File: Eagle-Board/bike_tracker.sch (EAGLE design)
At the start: 16 parts, among them J1 TRANSFLASH-LOCK

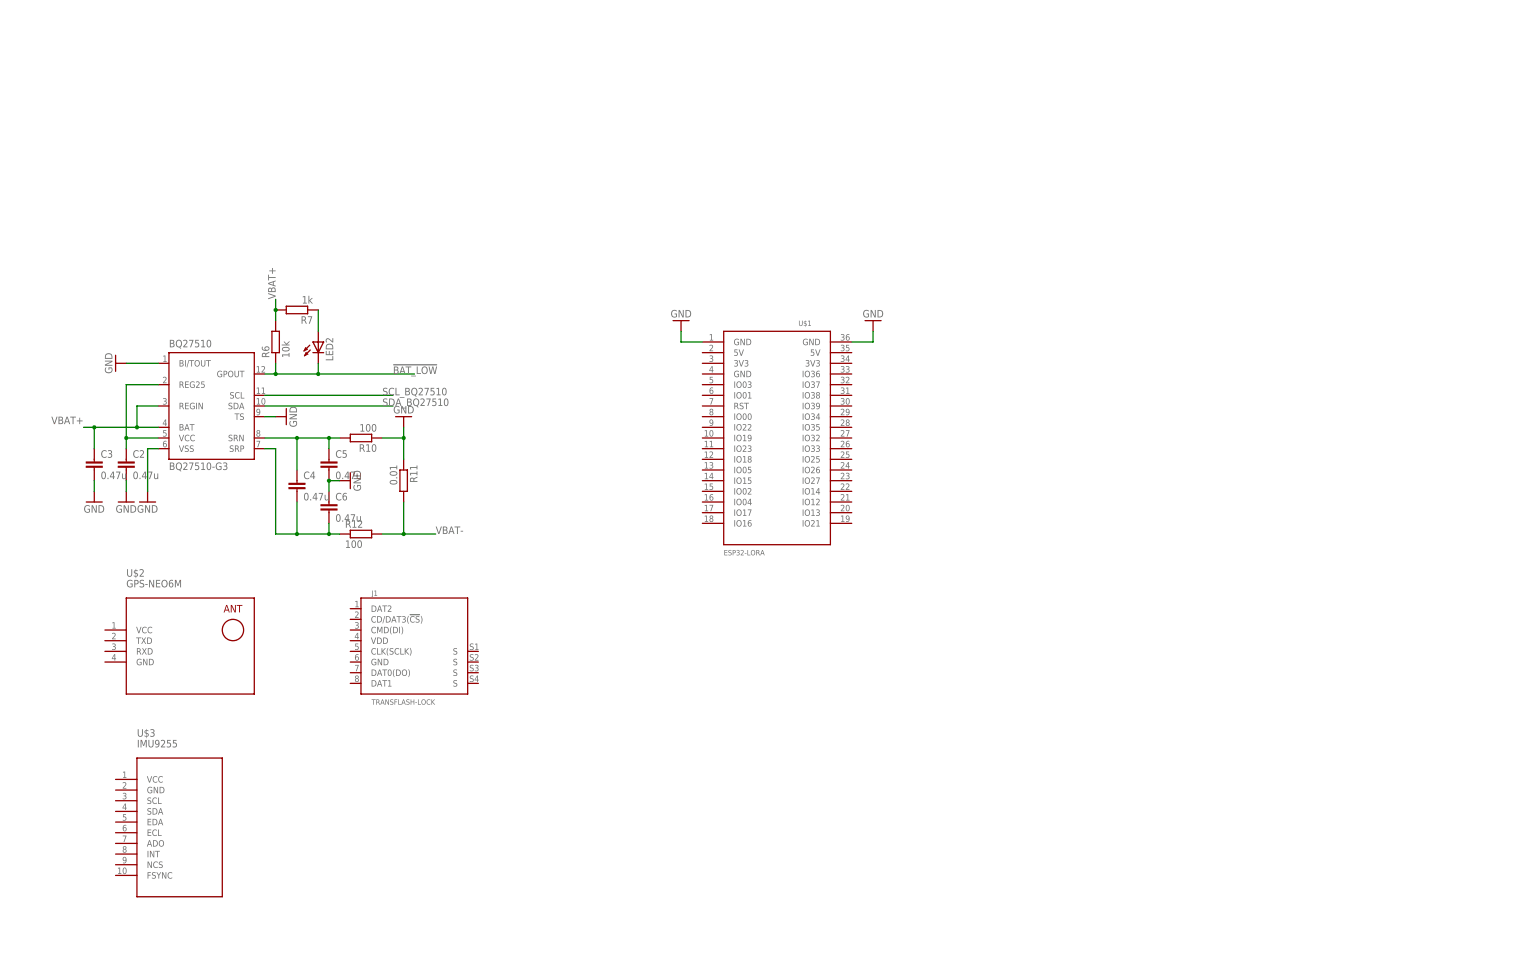
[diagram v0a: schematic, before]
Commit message: board design ready - revising and exporting for gerber - SeeedStudio Fusion files added
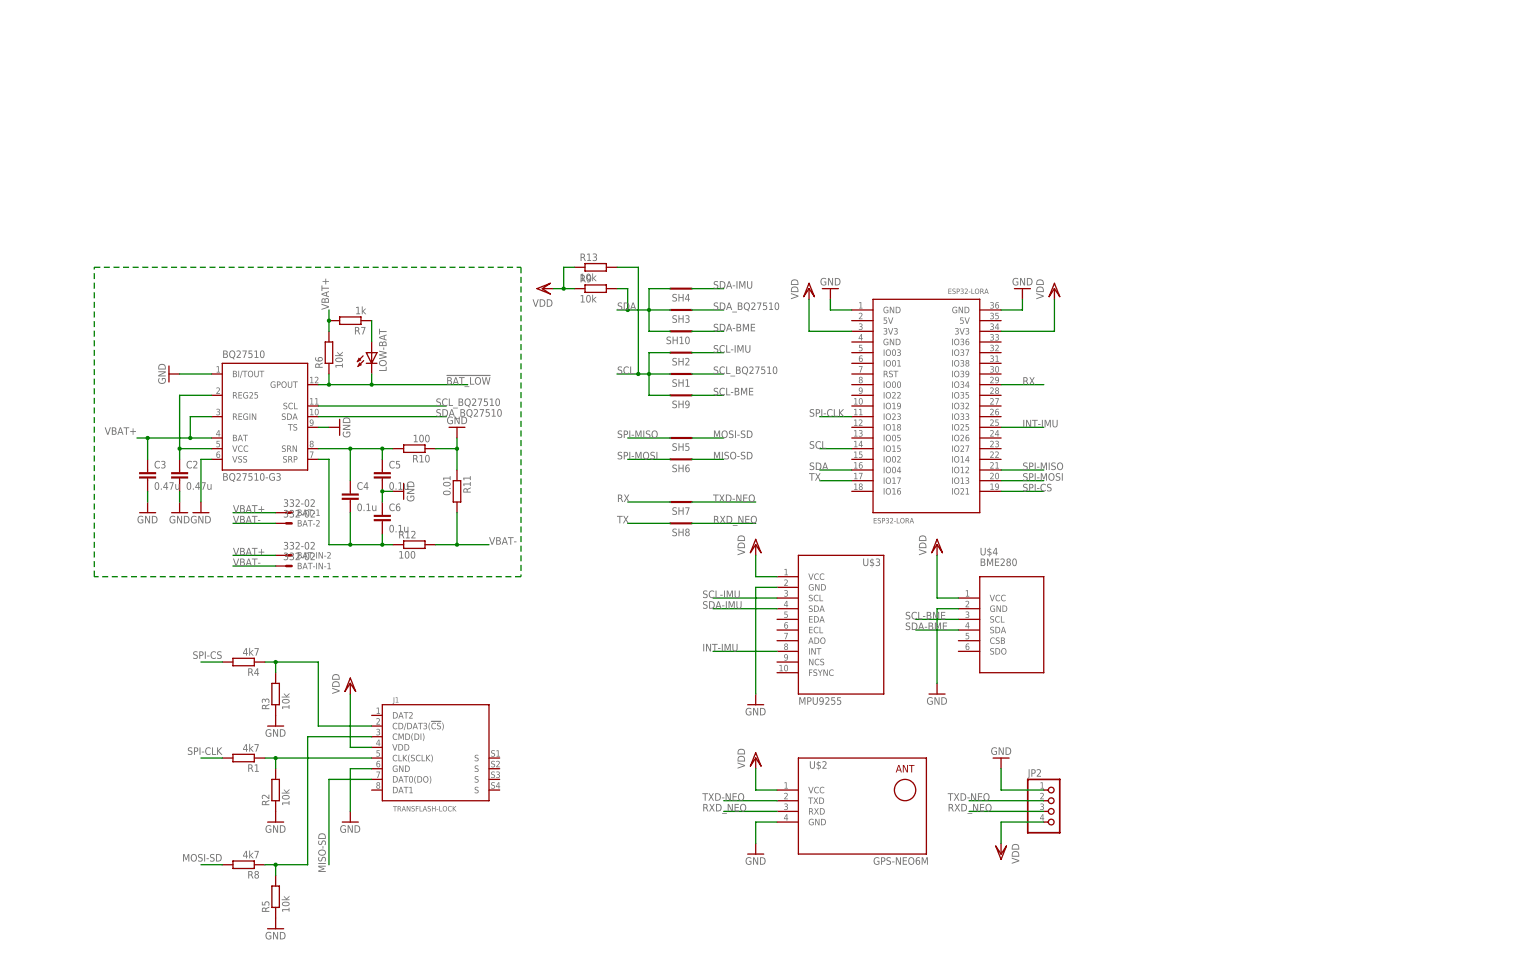
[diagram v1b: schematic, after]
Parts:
- removed LED2: (no value), led:LEDSML0805
- removed U$1: ESP32LORA, ESP32-DEVKITC:ESP32LORA
- added BAT, BAT-IN: 332-02, con-garry:332-02
- added ESP32-LORA: ESP32LORA, ESP32-DEVKITC:ESP32LORA
- added JP2: (no value), pinhead:PINHD-1X4
- added LOW-BAT: (no value), led:LEDSML0805
- added R1, R4, R8: 4k7, resistor:R-EU_R0603
- added R13, R2, R3, R5, R9: 10k, resistor:R-EU_R0603
- added SH1, SH10, SH2, SH3, SH4, SH5, SH6, SH7, SH8, SH9: SHORTT5, shorts:SHORTT5
- added U$4: BME280, diy-modules:BME280
- C4, C5, C6: value 0.47u -> 0.1u
- U$3: value IMU9255 -> MPU9255; device diy-modules:IMU9255 -> diy-modules:MPU9255
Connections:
- new net INT-IMU: ESP32-LORA.IO25, U$3.INT
- new net MISO-SD: J1.DAT0(DO), SH6.P$1
- new net MOSI-SD: R8.2, SH5.P$1
- new net N$1: J1.CLK(SCLK), R1.1, R2.2
- new net N$2: J1.CD/DAT3(!CS!), R3.2, R4.1
- new net N$3: J1.CMD(DI), R5.2, R8.1
- new net RX: ESP32-LORA.IO34, SH7.P$2
- new net RXD_NEO: JP2.3, SH8.P$1, U$2.RXD
- new net SCL: ESP32-LORA.IO15, R13.2, SH1.P$2, SH2.P$2, SH9.P$2
- new net SCL-BME: SH9.P$1, U$4.SCL
- new net SCL-IMU: SH2.P$1, U$3.SCL
- new net SDA: ESP32-LORA.IO04, R9.2, SH10.P$2, SH3.P$2, SH4.P$2
- new net SDA-BME: SH10.P$1, U$4.SDA
- new net SDA-IMU: SH4.P$1, U$3.SDA
- new net SPI-CLK: ESP32-LORA.IO23, R1.2
- new net SPI-CS: ESP32-LORA.IO21, R4.2
- new net SPI-MISO: ESP32-LORA.IO12, SH5.P$2
- new net SPI-MOSI: ESP32-LORA.IO13, SH6.P$2
- new net TX: ESP32-LORA.IO17, SH8.P$2
- new net TXD-NEO: JP2.2, SH7.P$1, U$2.TXD
- new net VDD: ESP32-LORA.3V3@3, ESP32-LORA.3V3@34, J1.VDD, JP2.4, R13.1, R9.1, U$2.VCC, U$3.VCC, U$4.VCC
- net !BAT_LOW: now also LOW-BAT.C; no longer LED2.C
- net GND: now also ESP32-LORA.GND@1, ESP32-LORA.GND@36, J1.GND, JP2.1, R2.1, R3.1, R5.1, U$2.GND, U$3.GND, U$4.GND; no longer U$1.GND@1, U$1.GND@36
- net N$9: now also LOW-BAT.A; no longer LED2.A
- net SCL_BQ27510: now also SH1.P$1
- net SDA_BQ27510: now also SH3.P$1
- net VBAT+: now also BAT-1.S, BAT-IN-2.S
- net VBAT-: now also BAT-2.S, BAT-IN-1.S
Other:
- moved on the sheet: BQ27510, C2, C3, C4, C5, C6, J1, R10, R11, R12, R6, R7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

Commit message: texas and switch libraries added final version with buttons and possibility to switch off/on external devices
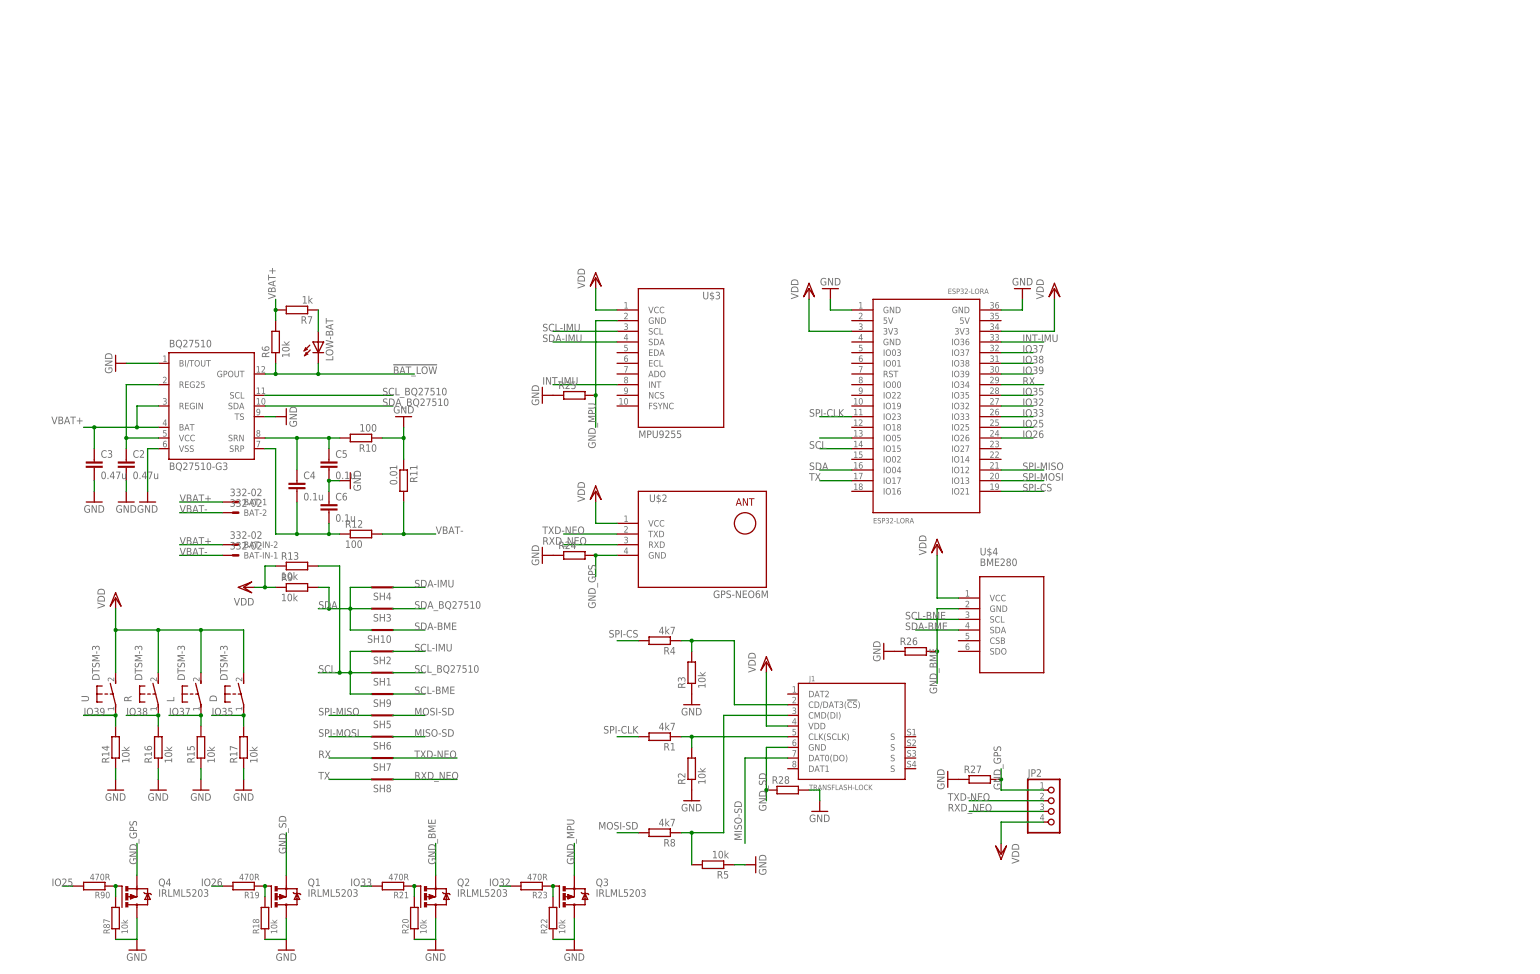
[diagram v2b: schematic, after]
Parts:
- added D, L, R, U: DTSM-3, switch-tact:DTSM-3
- added Q1, Q2, Q3, Q4: IRLML5203, transistor-power:IRLML5203
- added R14, R15, R16, R17: 10k, resistor:R-EU_R0603
- added R18, R20, R22, R87: 10k, ssmd:R_SMDR0603
- added R19, R21, R23, R90: 470R, ssmd:R_SMDR0603
- added R24, R25, R26, R27, R28: (no value), resistor:R-EU_R0201
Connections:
- new net GND_BME: Q2.S, R26.2, U$4.GND
- new net GND_GPS: JP2.1, Q4.S, R24.2, R27.2, U$2.GND
- new net GND_MPU: Q3.S, R25.2, U$3.GND
- new net GND_SD: J1.GND, Q1.S, R28.1
- new net IO25: ESP32-LORA.IO25, R90.2
- new net IO26: ESP32-LORA.IO26, R19.2
- new net IO32: ESP32-LORA.IO32, R23.2
- new net IO33: ESP32-LORA.IO33, R21.2
- new net IO35: D.1, ESP32-LORA.IO35, R17.2
- new net IO37: ESP32-LORA.IO37, L.1, R15.2
- new net IO38: ESP32-LORA.IO38, R.1, R16.2
- new net IO39: ESP32-LORA.IO39, R14.2, U.1
- new net N$12: ESP32-LORA.IO05
- new net N$4: Q4.G, R87.2, R90.1
- new net N$5: Q1.G, R18.2, R19.1
- new net N$6: Q2.G, R20.2, R21.1
- new net N$8: Q3.G, R22.2, R23.1
- net GND: now also Q1.D, Q2.D, Q3.D, Q4.D, R14.1, R15.1, R16.1, R17.1, R18.1, R20.1, R22.1, R24.1, R25.1, R26.1, R27.1, R28.2, R87.1; no longer J1.GND, JP2.1, U$2.GND, U$3.GND, U$4.GND
- net INT-IMU: now also ESP32-LORA.IO36; no longer ESP32-LORA.IO25
- net VDD: now also D.2, L.2, R.2, U.2
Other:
- moved on the sheet: BAT-1, BAT-2, BAT-IN-1, BAT-IN-2, BQ27510, C2, C3, C4, C5, C6, J1, LOW-BAT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

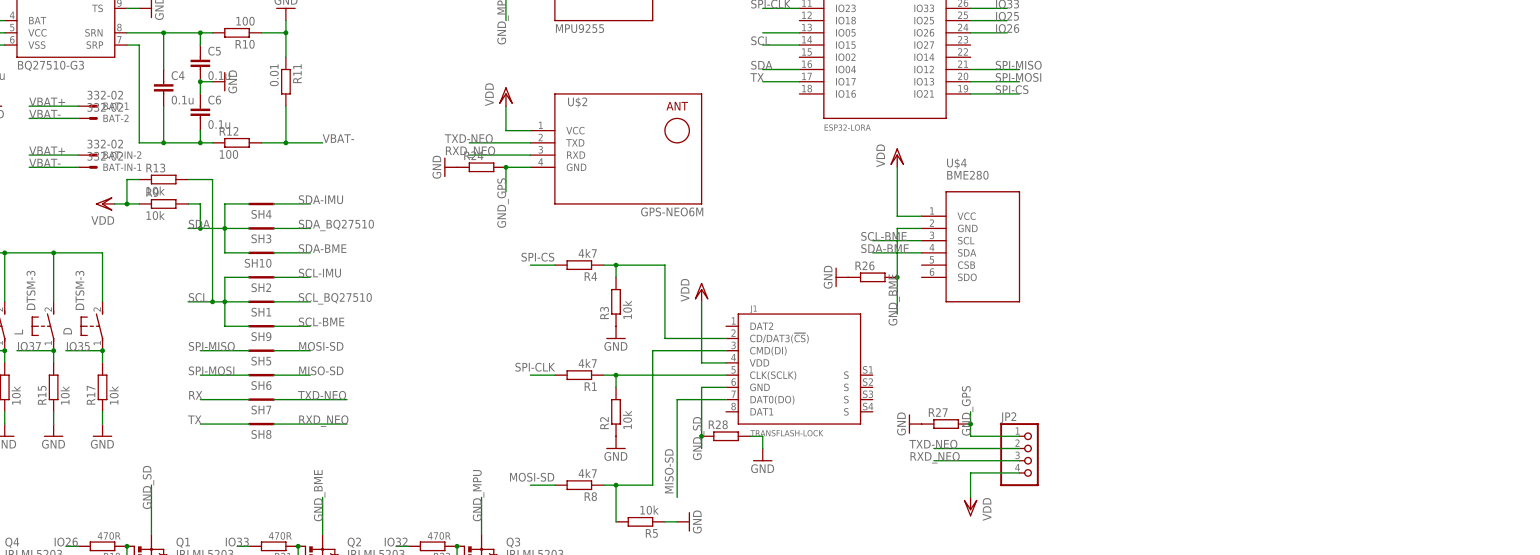
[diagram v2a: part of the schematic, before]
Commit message: updated rev1.1 -> added RTC chip (DS1339)
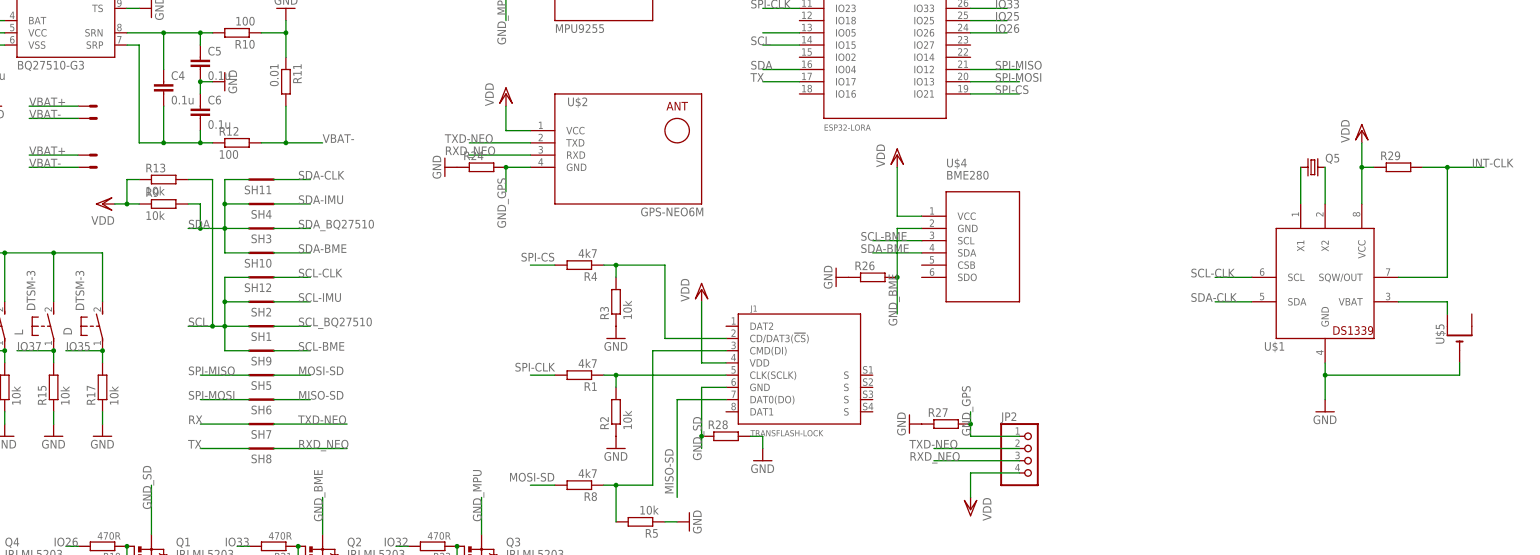
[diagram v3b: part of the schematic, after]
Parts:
- added Q5: (no value), adafruit:CRYSTALTC26H
- added R29: (no value), resistor:R-EU_R0603
- added SH11, SH12: SHORT, shorts:SHORT
- added U$1: DS1339, adafruit:DS1339
- added U$5: (no value), adafruit:CR1220SMT
- SH1, SH10, SH2, SH3, SH4, SH5, SH6, SH7, SH8, SH9: value SHORTT5 -> SHORT; device shorts:SHORTT5 -> shorts:SHORT
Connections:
- new net INT-CLK: R29.2, U$1.SQW/OUT
- new net N$10: Q5.1, U$1.X1
- new net N$13: Q5.2, U$1.X2
- new net N$15: U$1.VBAT, U$5.+
- new net SCL-CLK: SH12.P$1, U$1.SCL
- new net SDA-CLK: SH11.P$1, U$1.SDA
- net GND: now also U$1.GND, U$5.-
- net SCL: now also SH12.P$2
- net SDA: now also SH11.P$2
- net VDD: now also R29.1, U$1.VCC
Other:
- moved on the sheet: SH1, SH2, SH5, SH6, SH7, SH8, SH9

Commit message: revision v1.2
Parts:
- removed JP2: (no value), pinhead:PINHD-1X4
- removed R25, R26, R27: (no value), resistor:R-EU_R0201
- removed U$2: GPS-NEO6M, diy-modules:GPS-NEO6M
- removed U$3: MPU9255, diy-modules:MPU9255
- removed U$4: BME280, diy-modules:BME280
- added BAT1: XH414, microduino:BATTERY-TS414H
- added C1: 10uF, microduino:CAP_POL3528
- added C10, C11: 0.1uF, SparkFun-Capacitors:0.1UF-0603-25V-(+80/-20%)
- added C7: 0.1uF, microduino:CAP0603-CAP
- added C8, C9: 0.1uF, SparkFun-Capacitors:0.1UF-25V(+80/-20%)(0603)
- added D1: MBR0520, microduino:DIODE-SOD123
- added IC1: 24C00TS, microchip:24C00TS
- added IC2: BME280, bosch-bme280:BME280
- added IPEX: ANT-UMCC, microduino:ANT-UMCC
- added JP3: JUMPER-SMT_3_1-NC_TRACE_NO-SILK, SparkFun-Jumpers:JUMPER-SMT_3_1-NC_TRACE_NO-SILK
- added L1: (no value), microduino:INDUCTOR0603
- added R30, R31, R33: 1k, microduino:RESISTOR0603-RES
- added R32: null, microduino:RESISTOR0603-RES
- added R34: 10, microduino:RESISTOR0603-RES
- added R35, R36, R37: 10K, SparkFun-Resistors:10KOHM-1/10W-1%(0603)0603
- added R40, R41: 4.7k, SparkFun-Resistors:4.7KOHM-0603-1/10W-1%
- added R42: (no value), resistor:R-EU_R0201
- added SJ2: JUMPER_PAD-3-1&2_NC_BY_PASTE, SparkFun-Passives:JUMPER_PAD-3-1&2_NC_BY_PASTE
- added STATUS: green, microduino:LED0805
- added U$6: BLOX-NEO-6M, microduino:BLOX-NEO-6M
- added U1: MPU-9250, Testing:MPU-9250
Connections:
- new net !CS: R37.1, U1.!CS
- new net AD0/SDO: SJ2.3
- new net ADSD_STUB: SJ2.2, U1.AD0/SDO
- new net AUX_CL: U1.AUX_CL
- new net AUX_DA: U1.AUX_DA
- new net FSYNC: U1.FSYNC
- new net N$16: R30.2, STATUS.A
- new net N$17: STATUS.C, U$6.TIMEPULSE
- new net N$18: IPEX.ANT, L1.1, U$6.RF_IN
- new net N$19: R31.1, U$6.RXD1
- new net N$20: R32.1, U$6.MISO/CFG_COM1
- new net N$21: R33.1, U$6.MOSI/CFG_COM0
- new net N$22: BAT1.+, D1.C, U$6.V_BCKP
- new net N$23: L1.2, R34.2
- new net N$24: R34.1, U$6.RESERVED2, U$6.VCC_RF
- new net N$25: IC2.CSB, R40.1
- new net N$26: JP3.1, R41.1
- new net REGOUT: C8.1, U1.REGOUT
- new net RXD-NEO: R31.2
- new net SCL_GPS: IC1.SCL, U$6.SCL2
- new net SDA_GPS: IC1.SDA, U$6.SDA2
- new net SDO: IC2.SDO, JP3.2
- new net VDDIO: R35.2, R36.2, R37.2, U1.VDDIO
- net GND: now also C9.2, R42.2, SJ2.1; no longer R25.1, R26.1, R27.1
- net GND_BME: now also C10.2, C11.2, IC2.GND, JP3.3, R24.2; no longer R26.2, U$4.GND
- net GND_GPS: now also BAT1.-, C1.-, C7.2, IC1.GND, IPEX.GND1, IPEX.GND2, R32.2, R33.2, U$6.GND1, U$6.GND2, U$6.GND3, U$6.GND4, U$6.VDDUSB; no longer JP2.1, R24.2, R27.2, U$2.GND
- net GND_MPU: now also C8.2, R42.1, U1.GND; no longer R25.2, U$3.GND
- net INT-IMU: now also U1.INT; no longer U$3.INT
- net RXD_NEO: no longer JP2.3, U$2.RXD
- net SCL-BME: now also IC2.SCK; no longer U$4.SCL
- net SCL-IMU: now also R36.1, U1.SCL/SCLK; no longer U$3.SCL
- net SDA-BME: now also IC2.SDI; no longer U$4.SDA
- net SDA-IMU: now also R35.1, U1.SDA/SDI; no longer U$3.SDA
- net TXD-NEO: now also U$6.TXD1; no longer JP2.2, U$2.TXD
- net VDD: now also C1.+, C10.1, C11.1, C7.1, C9.1, D1.A, IC1.VCC, IC2.VDD, IC2.VDDIO, R30.1, R40.2, R41.2, U$6.VCC, U1.VDD; no longer JP2.4, U$2.VCC, U$3.VCC, U$4.VCC
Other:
- note added: "AD0 sets LSB of address"
- moved on the sheet: D, ESP32-LORA, J1, L, Q1, Q2, Q3, Q4, Q5, R, R1, R13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

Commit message: first commit rev1.2
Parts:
- removed R37: 10K, SparkFun-Resistors:10KOHM-1/10W-1%(0603)0603
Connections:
- removed net !CS: R37.1, U1.!CS
- removed net RXD_NEO: SH8.P$1
- net GND: no longer C9.2, SJ2.1
- net GND_MPU: now also C9.2, SJ2.1
- net RXD-NEO: now also SH8.P$1
- net VDDIO: no longer R37.2

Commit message: modified and cleaned for production
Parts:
- removed STATUS: green, microduino:LED0805
- removed U$6: BLOX-NEO-6M, microduino:BLOX-NEO-6M
- added GPS-STATUS: green, microduino:LED0805
- added NEO-GPS: BLOX-NEO-6M, microduino:BLOX-NEO-6M
- added R25, R26, R27, R37: (no value), resistor:R-EU_R0201
- C7: device microduino:CAP0603-CAP -> rcl:R-EU_R0603
- C8, C9: device SparkFun-Capacitors:0.1UF-25V(+80/-20%)(0603) -> resistor:C-USC0603K
- IC2: value BME280 -> BME280/680
- R18, R19, R22, R23, R87, R90: device ssmd:R_SMDR0603 -> resistor:R-EU_R0603
- R20, R21: device ssmd:R_SMDR0603 -> rcl:R-EU_R0603
- R30: device microduino:RESISTOR0603-RES -> resistor:R-EU_R0603
- R31, R32, R33, R34: device microduino:RESISTOR0603-RES -> rcl:R-EU_R0603
- R35, R36: device SparkFun-Resistors:10KOHM-1/10W-1%(0603)0603 -> resistor:R-EU_R0603
- U1: value MPU-9250 -> MPU-9250/5; device Testing:MPU-9250 -> invensense:MPU-9250
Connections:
- net ADSD_STUB renamed N$27
- net GND: now also R37.2
- net GND_GPS: now also NEO-GPS.GND1, NEO-GPS.GND2, NEO-GPS.GND3, NEO-GPS.GND4, NEO-GPS.VDDUSB, R37.1; no longer U$6.GND1, U$6.GND2, U$6.GND3, U$6.GND4, U$6.VDDUSB
- net GND_MPU: now also U1.PAD
- net N$10: now also U$1.X2; no longer U$1.X1
- net N$13: now also U$1.X1; no longer U$1.X2
- net N$16: now also GPS-STATUS.A; no longer STATUS.A
- net N$17: now also GPS-STATUS.C, NEO-GPS.TIMEPULSE; no longer STATUS.C, U$6.TIMEPULSE
- net N$18: now also NEO-GPS.RF_IN; no longer U$6.RF_IN
- net N$19: now also NEO-GPS.RXD1; no longer U$6.RXD1
- net N$20: now also NEO-GPS.MISO/CFG_COM1; no longer U$6.MISO/CFG_COM1
- net N$21: now also NEO-GPS.MOSI/CFG_COM0; no longer U$6.MOSI/CFG_COM0
- net N$22: now also NEO-GPS.V_BCKP; no longer U$6.V_BCKP
- net N$24: now also NEO-GPS.RESERVED2, NEO-GPS.VCC_RF; no longer U$6.RESERVED2, U$6.VCC_RF
- net SCL: now also R27.2
- net SCL_GPS: now also NEO-GPS.SCL2, R27.1; no longer U$6.SCL2
- net SDA: now also R26.2
- net SDA_GPS: now also NEO-GPS.SDA2, R26.1; no longer U$6.SDA2
- net TXD-NEO: now also NEO-GPS.TXD1; no longer U$6.TXD1
- net VDD: now also NEO-GPS.VCC, R25.1; no longer U$6.VCC
- net VDDIO: now also R25.2, U1.RESV
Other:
- moved on the sheet: BAT1, BQ27510, C1, C10, C11, C2, C3, C4, C5, C6, C7, C8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
